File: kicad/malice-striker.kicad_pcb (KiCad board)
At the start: 4 copper layers, 57 x 74.8 mm, 66 parts, among them J1 Conn_01x02_Female, J2 Conn_01x02_Female, J3 Conn_01x02_Female, U1 TL072, U2 LT1054, U3 OP07, U4 TL072

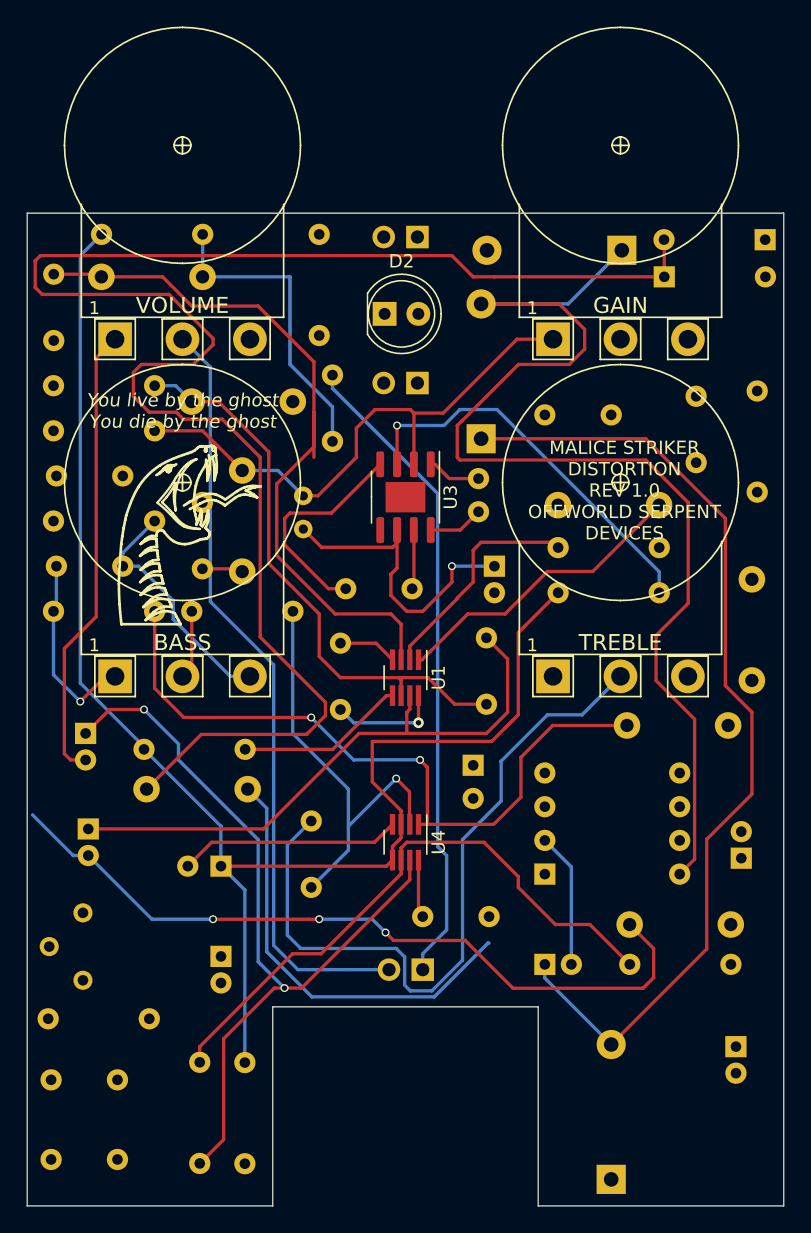
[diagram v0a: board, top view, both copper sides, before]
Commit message: modified pcb size a bit to fit stomp switch breakout
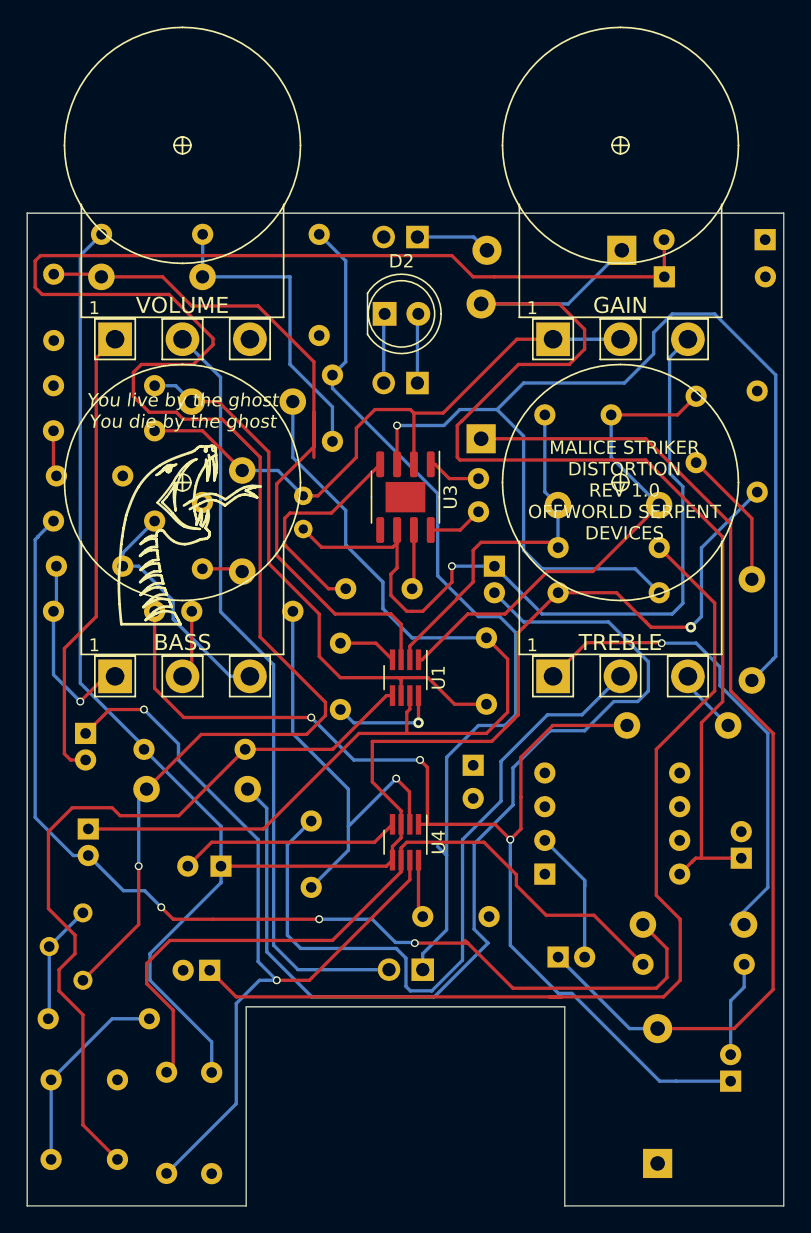
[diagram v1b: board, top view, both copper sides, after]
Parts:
- moved D4 3.70 mm to (65.5, 105.8)
- moved C24 2.63 mm to (71.0, 99.6), turned to 90 degrees
- moved R16 2.61 mm to (31.9, 99.0)
- moved R23 2.61 mm to (28.5, 106.5)
- moved C3 1.35 mm to (31.8, 91.2), turned to 180 degrees
- moved C9 1.14 mm to (58.0, 90.2)
- moved R22 1.00 mm to (64.4, 90.8)
- moved R18 1.00 mm to (68.2, 87.8)
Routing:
- net Net-(C3-Pad1): track 0.00 -> 74.6 mm
- net Net-(R6-Pad1): track 29.8 -> 84.5 mm
- net Net-(C17-Pad1): track 12.8 -> 58.5 mm
- net Net-(C12-Pad2): track 32.7 -> 76.0 mm
- net Net-(C11-Pad1): track 24.3 -> 61.2 mm
- net Net-(R18-Pad2): track 0.00 -> 36.4 mm, vias 0 -> 1
- net Net-(C24-Pad1): track 53.7 -> 85.0 mm, vias 2 -> 3
- net VREF: track 114.7 -> 142.2 mm, vias 0 -> 1
- net Net-(C19-Pad1): track 44.5 -> 71.6 mm
- net Net-(C20-Pad2): track 57.3 -> 81.2 mm
- net INPUT: track 49.1 -> 68.3 mm
- net Net-(D5-Pad1): track 125.9 -> 142.3 mm, vias 0 -> 1
- net Net-(C15-Pad1): track 0.00 -> 15.3 mm
- net Net-(C5-Pad1): track 23.0 -> 38.2 mm
- net Net-(C6-Pad1): track 0.00 -> 10.5 mm
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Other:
- outline, holes or cut-outs redrawn

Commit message: added connections for LED and input/output grounds
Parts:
- added 9VOUT: Conn_01x01_Female, Connector_PinSocket_2.54mm:PinSocket_1x01_P2.54mm_Vertical, B.Cu at (73.2, 43.8)
- added J5: GNDOUT, Connector_PinSocket_2.54mm:PinSocket_1x01_P2.54mm_Vertical, B.Cu at (61.0, 99.0)
- added J6: INPUTGND, Connector_PinSocket_2.54mm:PinSocket_1x01_P2.54mm_Vertical, B.Cu at (61.0, 102.8)
- added J7: OUTPUTGND, Connector_PinSocket_2.54mm:PinSocket_1x01_P2.54mm_Vertical, B.Cu at (61.0, 106.5)
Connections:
- net Net-(C4-Pad1) renamed 9VOUT
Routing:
- net 9VOUT: track 89.5 -> 103.8 mm
- net Net-(R6-Pad1): track 84.5 -> 86.0 mm

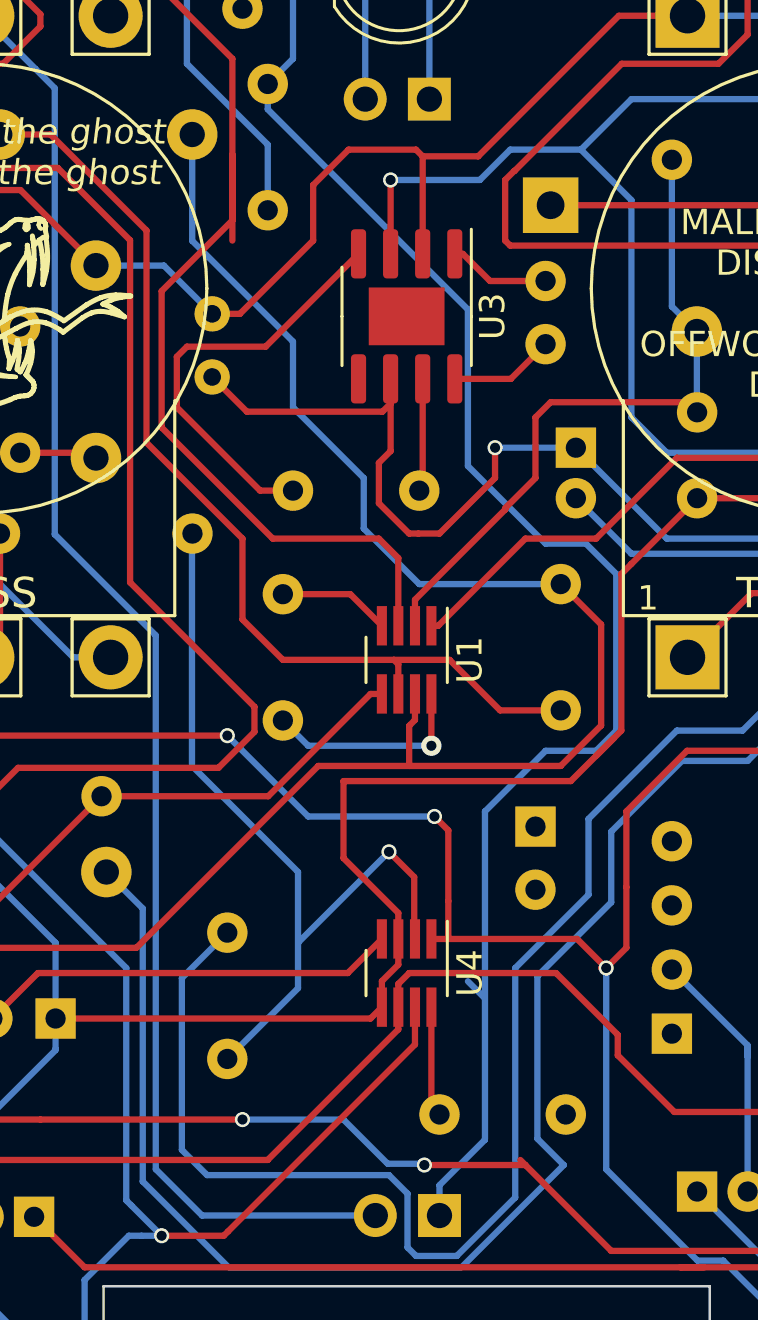
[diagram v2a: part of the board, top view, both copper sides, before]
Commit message: cleaned up PCB a bit
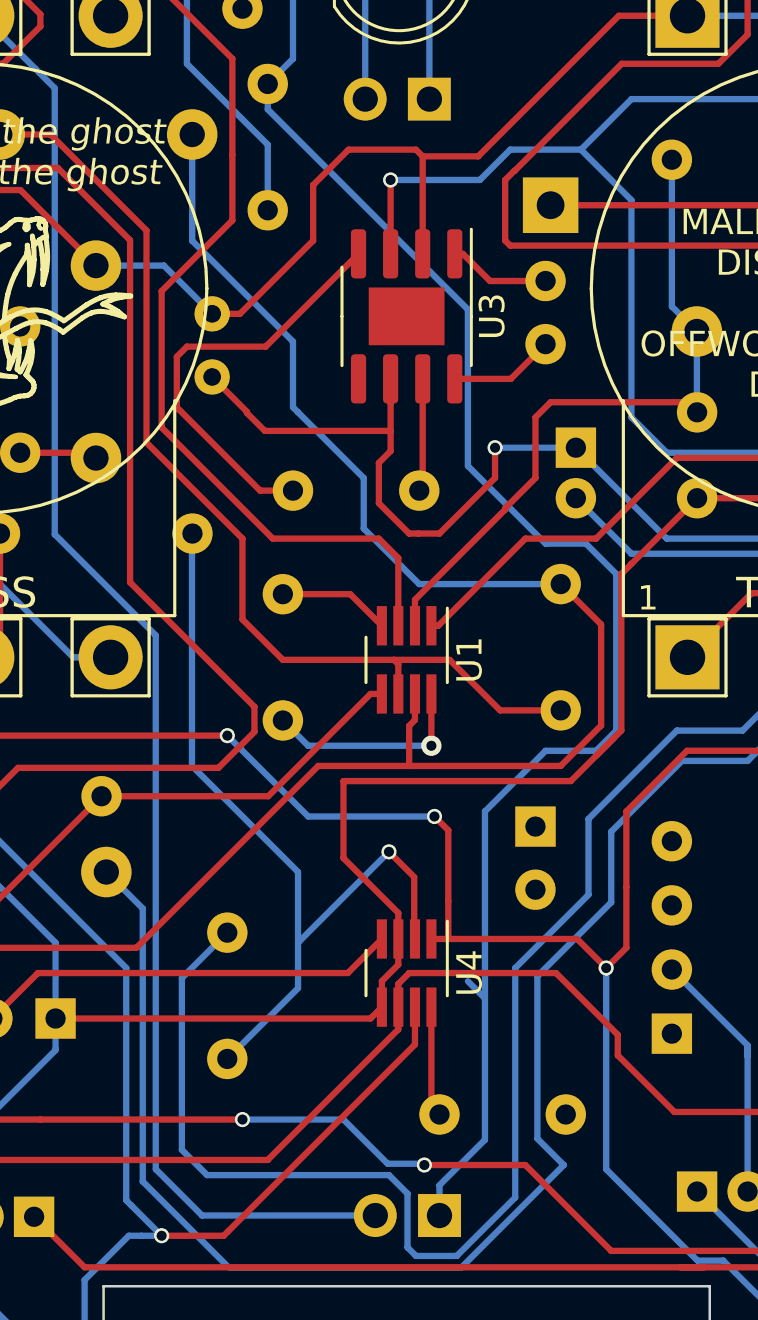
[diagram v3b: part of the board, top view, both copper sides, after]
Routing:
- net Net-(C2-Pad1): track 55.7 -> 52.3 mm
